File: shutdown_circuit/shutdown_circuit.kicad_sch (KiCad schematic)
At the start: 0 parts

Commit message: Updated KiCad schematic
...to include mosfet as a relay replacement & (some) HAT standard implementations such as I2C EEPROM
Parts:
- added C1: 1000uF, symbol Device:C_Polarized
- added D2, D3, D4, D?: 1N4007, Diode_THT:D_DO-41_SOD81_P10.16mm_Horizontal, symbol Diode:1N4007
- added D5: 1N5822, Diode_THT:D_DO-201AD_P15.24mm_Horizontal, symbol Diode:1N5822
- added D?: LED, symbol Device:LED
- added J1: Raspberry_Pi_4, symbol Connector:Raspberry_Pi_2_3
- added L1: 100uH, symbol pspice:INDUCTOR
- added Q?: Q_NMOS_GDS, symbol Device:Q_NMOS_GDS
- added R1, R2: 1k, symbol Device:R_US
- added R? (x4): 4k7, symbol Device:R_US
- added R?: 330, symbol Device:R_US
- added R?: 10, symbol Device:R_US
- added U1, U4: 4N35, Package_DIP:DIP-6_W7.62mm, symbol Isolator:4N35
- added U2: LM2576HVS-3.3, Package_TO_SOT_SMD:TO-263-5_TabPin3, symbol Regulator_Switching:LM2576HVS-3.3
- added U3: ATtiny85-20P, Package_DIP:DIP-8_W7.62mm, symbol MCU_Microchip_ATtiny:ATtiny85-20P
- added U5: DS1307+, Package_DIP:DIP-8_W7.62mm, symbol Timer_RTC:DS1307+
- added U?: CAT24C128, symbol Memory_EEPROM:CAT24C128
- added Y?: 32.768 kHz, symbol Device:Crystal
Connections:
- new net: D3.1 (K), D4.1 (K), R?.1, U1.5
- new net: D4.2 (A), J1.16 (GPIO23)
- new net: Q?.1 (G), R?.2
- new net: D2.2 (A), Q?.2 (D)
- new net: J1.3 (SDA/GPIO2), R?.2, U3.5 (AREF/PB0), U5.5 (SDA)
- new net: R2.2, U4.1
- new net: J1.18 (GPIO24), R?.1, U4.5
- new net: J1.5 (SCL/GPIO3), R?.2, U3.7 (PB2), U5.6 (SCL)
- new net: D2.1 (K), D?.1 (K), U2.1 (VIN)
- new net: D?.2 (A), R?.2
- new net: R1.2, U1.1
- new net: D5.1 (K), L1.1, U2.2 (OUT)
- new net: J1.27 (ID_SD/GPIO0), U?.5 (SDA)
- new net: J1.28 (ID_SC/GPIO1), U?.6 (SCL)
- new net: R?.1, U3.3 (XTAL2/PB4)
- new net: U5.1 (X1), Y?.1
- new net: U5.2 (X2), Y?.2
- new net: D3.2 (A), U3.2 (XTAL1/PB3)
- new net +12V: D?.2 (A), Q?.3 (S), R1.1, R2.1
- new net +3.3V: R?.2
- new net +3v3: C1.1, L1.2, R?.1, R?.1, R?.1, R?.2, U2.4 (FB), U3.8 (VCC), U?.8 (VCC)
- new net +5V: J1.2 (5V), J1.4 (5V), U5.8 (VCC)
- new net +BATT: U5.3 (VBAT)
- new net GND: C1.2, D5.2 (A), D?.1 (K), J1.14 (GND), J1.20 (GND), J1.25 (GND), J1.30 (GND), J1.34 (GND), J1.39 (GND), J1.6 (GND), J1.9 (GND), U1.2, U1.4, U2.3 (GND), U2.5 (~{ON}/OFF), U3.4 (GND), U4.2, U4.4, U5.4 (GND), U?.4 (GND)
- no-connect marks 0 -> 28
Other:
- note added: "3v0 Coin Cell"
- note added: "ACC"
- note added: "BAT"
- note added: "Headlight Detection"
- note added: "Headlights"
- note added: "RPi 4"
- note added: "RTC"
- note added: "Shutdown Controller"
- title: (none) -> PILOT Drive Raspberry Pi HAT

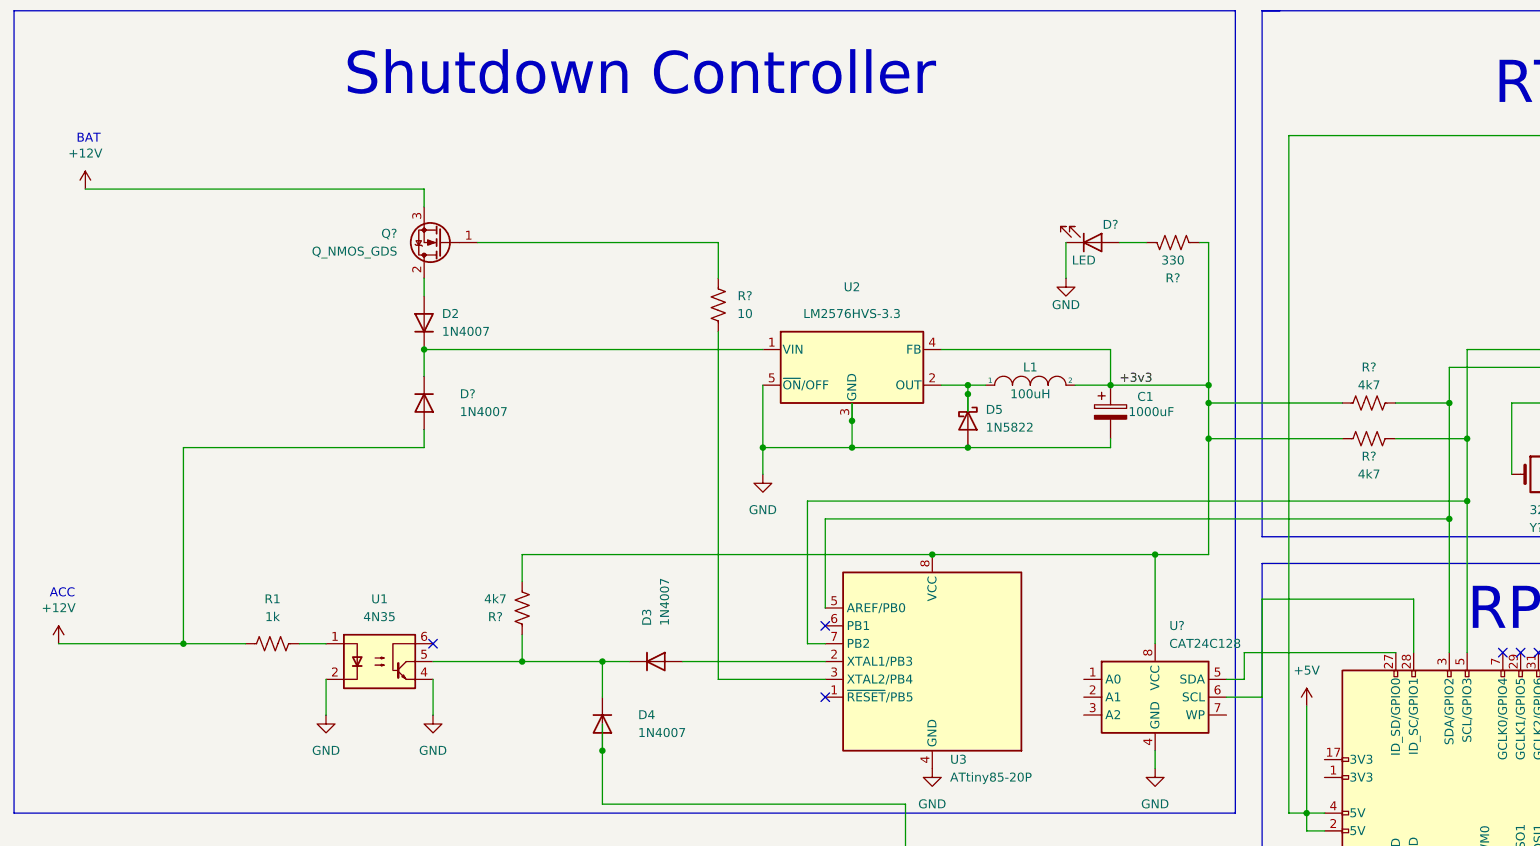
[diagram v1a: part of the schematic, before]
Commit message: schematic update
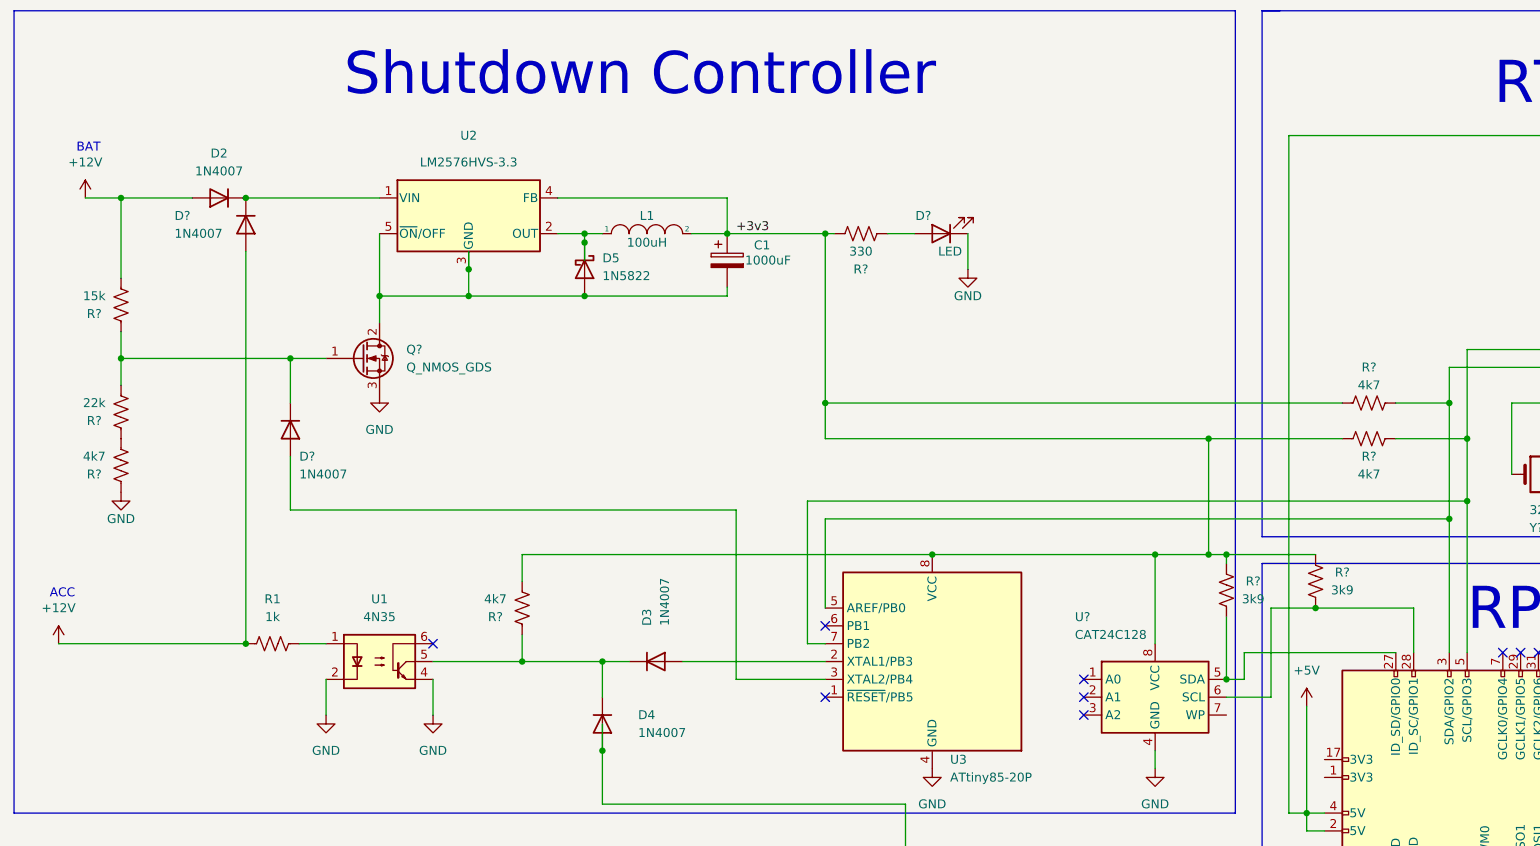
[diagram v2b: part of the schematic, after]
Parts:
- removed Q?: Q_NMOS_GDS, symbol Device:Q_NMOS_GDS
- removed R?: 10, symbol Device:R_US
- added D?: 1N4007, Diode_THT:D_DO-41_SOD81_P10.16mm_Horizontal, symbol Diode:1N4007
- added Q?: Q_NMOS_GDS, symbol Device:Q_NMOS_GDS
- added R?: 15k, symbol Device:R_US
- added R? (x2): 3k9, symbol Device:R_US
- added R?: 22k, symbol Device:R_US
- added R?: 4k7, symbol Device:R_US
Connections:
- net +12V: now also D2.2 (A), R?.2
- net +3v3: now also R?.2, R?.2
- net GND: now also Q?.3 (S), R?.1; no longer C1.2, D5.2 (A), U2.3 (GND), U2.5 (~{ON}/OFF)
- net at J1.27 (ID_SD/GPIO0), U?.5 (SDA): now also R?.1
- net at J1.28 (ID_SC/GPIO1), U?.6 (SCL): now also R?.1
- net at U3.3 (XTAL2/PB4): now also D?.2 (A)
- new net: D?.1 (K), Q?.1 (G), R?.1, R?.2
- new net: C1.2, D5.2 (A), Q?.2 (D), U2.3 (GND), U2.5 (~{ON}/OFF)
- new net: R?.1, R?.2
- no-connect marks 28 -> 31
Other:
- moved on the sheet: C1, D2, D5, D?, L1, R?, U2

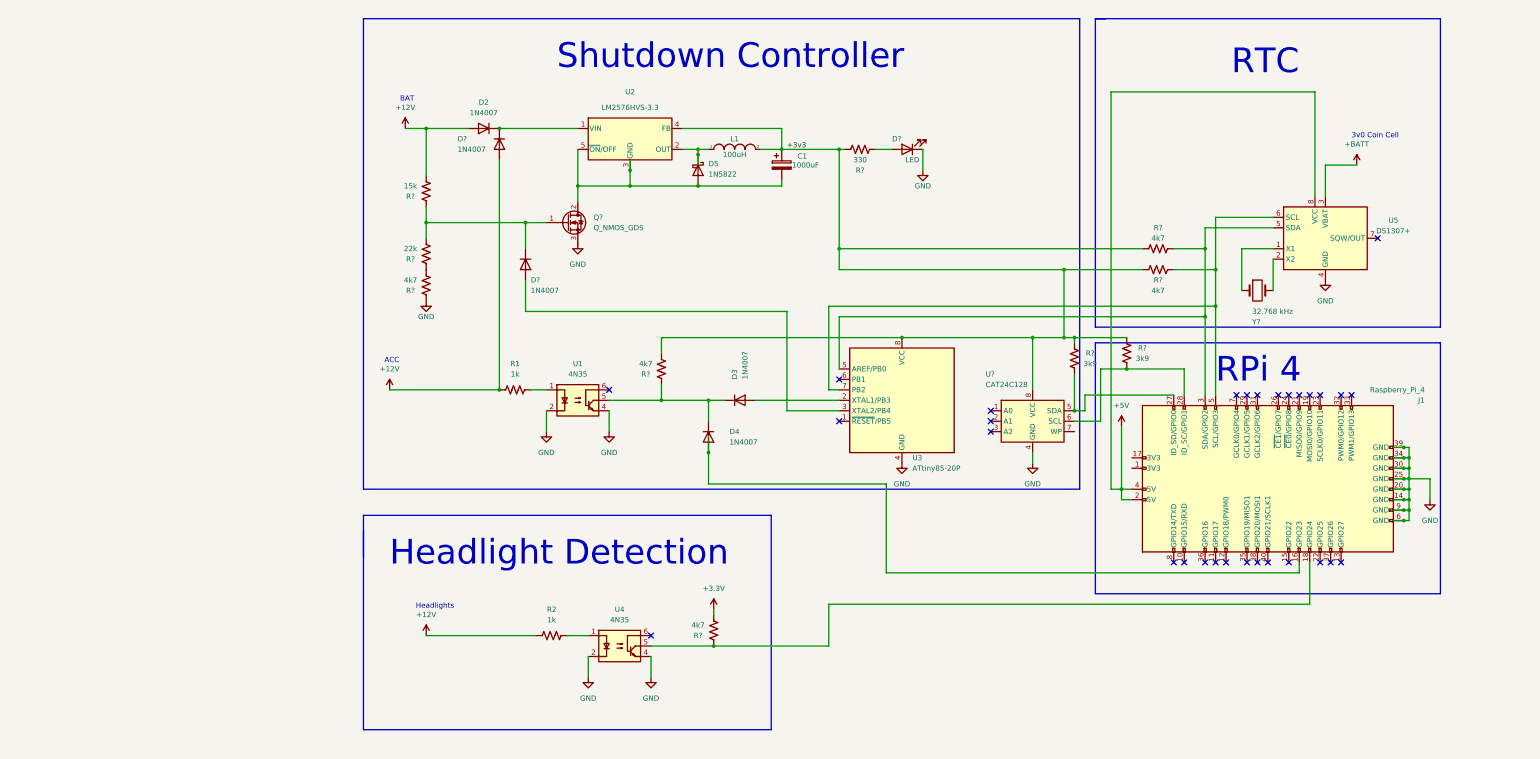
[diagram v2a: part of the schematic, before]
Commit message: Made schematic conform to HAT standards + added nets
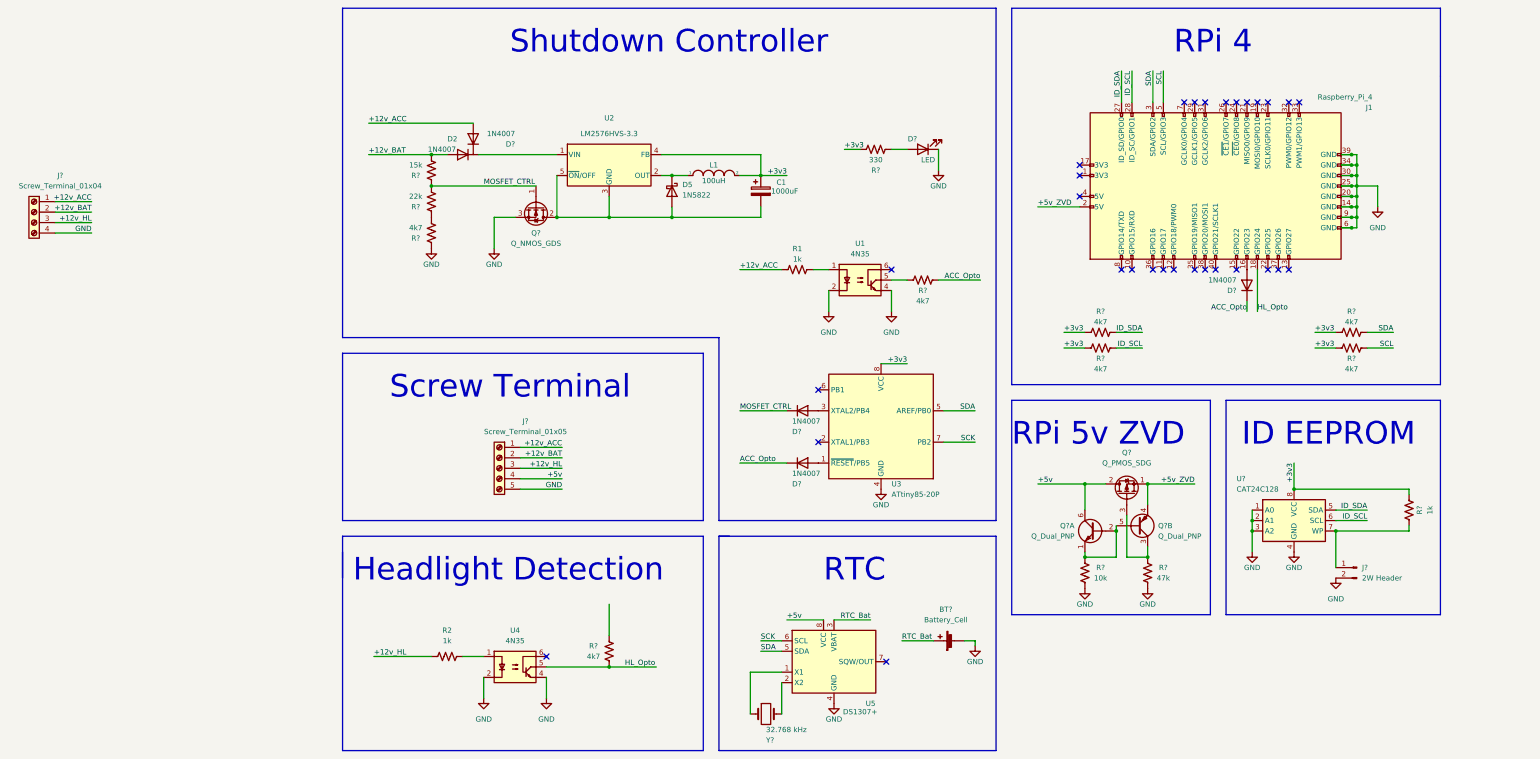
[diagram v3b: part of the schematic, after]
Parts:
- removed D3, D4, D? (x2): 1N4007, Diode_THT:D_DO-41_SOD81_P10.16mm_Horizontal, symbol Diode:1N4007
- removed R? (x2): 3k9, symbol Device:R_US
- removed R? (x2): 4k7, symbol Device:R_US
- removed U?: CAT24C128, symbol Memory_EEPROM:CAT24C128
- added BT?: Battery_Cell, symbol Device:Battery_Cell
- added D? (x4): 1N4007, Diode_THT:D_DO-41_SOD81_P10.16mm_Horizontal, symbol Diode:1N4007
- added J?: Screw_Terminal_01x05, symbol Connector:Screw_Terminal_01x05
- added J?: 2W Header, symbol Connector:Conn_01x02_Male
- added J?: Screw_Terminal_01x04, symbol Connector:Screw_Terminal_01x04
- added Q? (x2): Q_Dual_PNP, symbol Device:Q_Dual_NPN_PNP_E1B1C2E2B2C1
- added Q?: Q_PMOS_SDG, symbol Device:Q_PMOS_SDG
- added R? (x4): 4k7, symbol Device:R_US
- added R?: 1k, symbol Device:R_US
- added R?: 47k, symbol Device:R_US
- added R?: 10k, symbol Device:R_US
- added U?: CAT24C128, symbol Memory_EEPROM:CAT24C128
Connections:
- net +3v3: now also R?.2, R?.2, R?.2, R?.2, R?.2, U?.8 (VCC); no longer R?.2
- net GND: now also BT?.2 (-), J?.2 (Pin_2), J?.4 (Pin_4), J?.5 (Pin_5), R?.2, R?.2, U?.1 (A0), U?.2 (A1), U?.3 (A2), U?.4 (GND)
- net MOSFET_CTRL: now reaches Q?.1 (G), R?.1, R?.2
- net MOSFET_CTRL: now also D?.1 (K)
- net at U3.3 (XTAL2/PB4): now also D?.2 (A)
- net at U1.5: now also R?.2; no longer R?.1
- net at J1.16 (GPIO23): now also D?.2 (A)
- net ID_SCL: now reaches J1.28 (ID_SC/GPIO1)
- net ID_SCL: now also R?.1, U?.6 (SCL)
- net SDA: now reaches J1.3 (SDA/GPIO2), U3.5 (AREF/PB0), U5.5 (SDA)
- net SDA: now also R?.1
- net HL_Opto: now reaches J1.18 (GPIO24), R?.1, U4.5
- net SCK: now reaches U3.7 (PB2), U5.6 (SCL)
- net SCK: no longer J1.5 (SCL/GPIO3)
- net ID_SDA: now reaches J1.27 (ID_SD/GPIO0)
- net ID_SDA: now also R?.1, U?.5 (SDA)
- net at U3.1 (~{RESET}/PB5): now also D?.2 (A)
- net +12V renamed +12v_BAT
- net +12v_BAT: now also J?.2 (Pin_2), J?.2 (Pin_2); no longer R1.1, R2.1
- net +3.3V: no longer names the net of R?.2
- removed net +5V: J1.2 (5V), J1.4 (5V), U5.8 (VCC)
- net +BATT renamed RTC_Bat
- net RTC_Bat: now also BT?.1 (+)
- new net: J?.1 (Pin_1), R?.1, U?.7 (WP)
- new net: Q?.1 (E1), Q?.2 (B1), Q?.5 (B2), R?.1
- new net: Q?.3 (C2), Q?.3 (G), R?.1
- new net +12v_ACC: D?.2 (A), J?.1 (Pin_1), J?.1 (Pin_1), R1.1
- new net +12v_HL: J?.3 (Pin_3), J?.3 (Pin_3), R2.1
- new net +5v: J?.4 (Pin_4), Q?.2 (D), Q?.6 (C1), U5.8 (VCC)
- new net +5v_ZVD: J1.2 (5V), Q?.1 (S), Q?.4 (E2)
- new net ACC_Opto: D?.1 (K), D?.1 (K), R?.1
- new net SCL: J1.5 (SCL/GPIO3), R?.1
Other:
- note added: "ID EEPROM"
- note added: "RPi 5v ZVD"
- note added: "Screw Terminal"
- note removed: "3v0 Coin Cell"
- note removed: "ACC"
- note removed: "BAT"
- note removed: "Headlights"
- moved on the sheet: C1, D2, D5, D?, J1, L1, Q?, R1, R2, R?, U1, U2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

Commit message: Schematic, PCB, and netlist upload
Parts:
- removed J?: Screw_Terminal_01x05, symbol Connector:Screw_Terminal_01x05
- removed J?: 2W Header, symbol Connector:Conn_01x02_Male
- removed J?: Screw_Terminal_01x04, symbol Connector:Screw_Terminal_01x04
- removed R2: 1k, symbol Device:R_US
- removed R?: 4k7, symbol Device:R_US
- removed U1, U4: 4N35, Package_DIP:DIP-6_W7.62mm, symbol Isolator:4N35
- added D10: 1N4007, pilot_footprints:1N4007FLTR, symbol Diode:1N4007
- added D8, D9: RB520S30T1G, pilot_footprints:schottky_diodes, symbol Device:D_Schottky
- added J1: Screw_Terminal_01x06, pilot_footprints:screw_term_6, symbol Connector:Screw_Terminal_01x06
- added J3, J4: 6W Header, Connector_PinHeader_2.54mm:PinHeader_1x06_P2.54mm_Vertical, symbol Connector:Conn_01x06_Male
- added R16, R5: 4k7, Resistor_SMD:R_0603_1608Metric_Pad0.98x0.95mm_HandSolder, symbol Device:R_US
- added R4: 1k, Resistor_SMD:R_0603_1608Metric_Pad0.98x0.95mm_HandSolder, symbol Device:R_US
- added U1, U4: SFH617A-1, Package_DIP:DIP-4_W7.62mm, symbol Isolator:SFH617A-1
- BT1: renamed from BT?; footprint (none) -> Battery:BatteryHolder_Keystone_106_1x20mm
- C1: footprint (none) -> pilot_footprints:100uF_Cap
- D1: renamed from D2; footprint Diode_THT:D_DO-41_SOD81_P10.16mm_Horizontal -> pilot_footprints:1N4007FLTR
- D2, D4, D5, D7: renamed from D?; footprint Diode_THT:D_DO-41_SOD81_P10.16mm_Horizontal -> pilot_footprints:1N4007FLTR
- D3: renamed from D5; footprint Diode_THT:D_DO-201AD_P15.24mm_Horizontal -> pilot_footprints:1N4007FLTR
- D6: renamed from D?; footprint (none) -> LED_SMD:LED_0603_1608Metric_Pad1.05x0.95mm_HandSolder
- J2: renamed from J1; footprint (none) -> Connector_PinSocket_2.54mm:PinSocket_2x20_P2.54mm_Vertical
- L1: footprint (none) -> pilot_footprints:induct_100uH
- Q1: renamed from Q?; footprint (none) -> Package_TO_SOT_THT:TO-220-3_Vertical
- Q2: renamed from Q?; footprint (none) -> pilot_footprints:pnp_pair
- Q3: renamed from Q?; footprint (none) -> pilot_footprints:zvd_mosfet
- R1, R10, R11, R12, R13, R14, R15, R2, R3, R7, R8, R9: renamed from R?; footprint (none) -> Resistor_SMD:R_0603_1608Metric_Pad0.98x0.95mm_HandSolder
- R6: renamed from R1; footprint (none) -> Resistor_SMD:R_0603_1608Metric_Pad0.98x0.95mm_HandSolder
- U5: renamed from U3; footprint Package_DIP:DIP-8_W7.62mm -> Package_SO:SOIC-8W_5.3x5.3mm_P1.27mm
- U6: renamed from U?; footprint (none) -> Package_SO:TSSOP-8_4.4x3mm_P0.65mm
- Y1: renamed from Y?; footprint (none) -> Crystal:Crystal_SMD_3215-2Pin_3.2x1.5mm
- renumbered U5 to U3
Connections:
- net SCK is gone; now on net SCL: U3.6 (SCL), U5.7 (PB2)
- net +12v_ACC: now also J1.1 (Pin_1)
- net +12v_BAT: now also J1.2 (Pin_2)
- net +12v_HL: now also J1.3 (Pin_3), R4.1
- net +3v3: now also R8.1, D8.2 (A), D9.2 (A), R5.1; no longer R15.2, U5.8 (VCC), U6.8 (VCC)
- net +5v: now also J1.4 (Pin_4); no longer U3.8 (VCC)
- net +5v_ZVD: now also J2.4 (5V), U3.8 (VCC)
- net ACC_Opto: now also R8.2, U4.4; no longer R8.1
- net GND: now also D10.2 (A), J3.6 (Pin_6), J4.2 (Pin_2), J4.5 (Pin_5), U1.2, U1.3, U4.2, U4.3
- net HL_Opto: now also R5.2, U1.4
- net ID_SCL: now also J4.3 (Pin_3)
- net ID_SDA: now also J4.4 (Pin_4)
- net SCL: now also J3.4 (Pin_4)
- net at R15.1, U6.7 (WP): now also J4.1 (Pin_1)
- net RESET: now reaches D5.2 (A), U5.1 (~{RESET}/PB5)
- net RESET: now also J3.5 (Pin_5)
- net at D1.1 (K), U2.1 (VIN): now also D2.1 (K)
- net at R6.2: now also U4.1
- net +3v3_RPi: now reaches J2.1 (3V3)
- net +3v3_RPi: now also R16.1
- net BACKUP_BTN: now reaches J2.11 (GPIO17)
- net BACKUP_BTN: now also J1.5 (Pin_5), R16.2
- net MISO: now reaches U5.6 (PB1)
- net MISO: now also J3.3 (Pin_3)
- net SDA renamed MOSI
- net MOSI: now also J3.2 (Pin_2)
- new net: R4.2, U1.1
- new net: D9.1 (K), J4.6 (Pin_6), R15.2, U6.8 (VCC)
- new net: D10.1 (K), J1.6 (Pin_6)
- new net ATTINY_VCC: D8.1 (K), J3.1 (Pin_1), U5.8 (VCC)
- no-connect marks 31 -> 24
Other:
- moved on the sheet: C1, D1, D2, D3, D4, D5, D6, L1, Q1, R1, R10, R11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
